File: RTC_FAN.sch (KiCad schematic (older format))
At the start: 13 parts

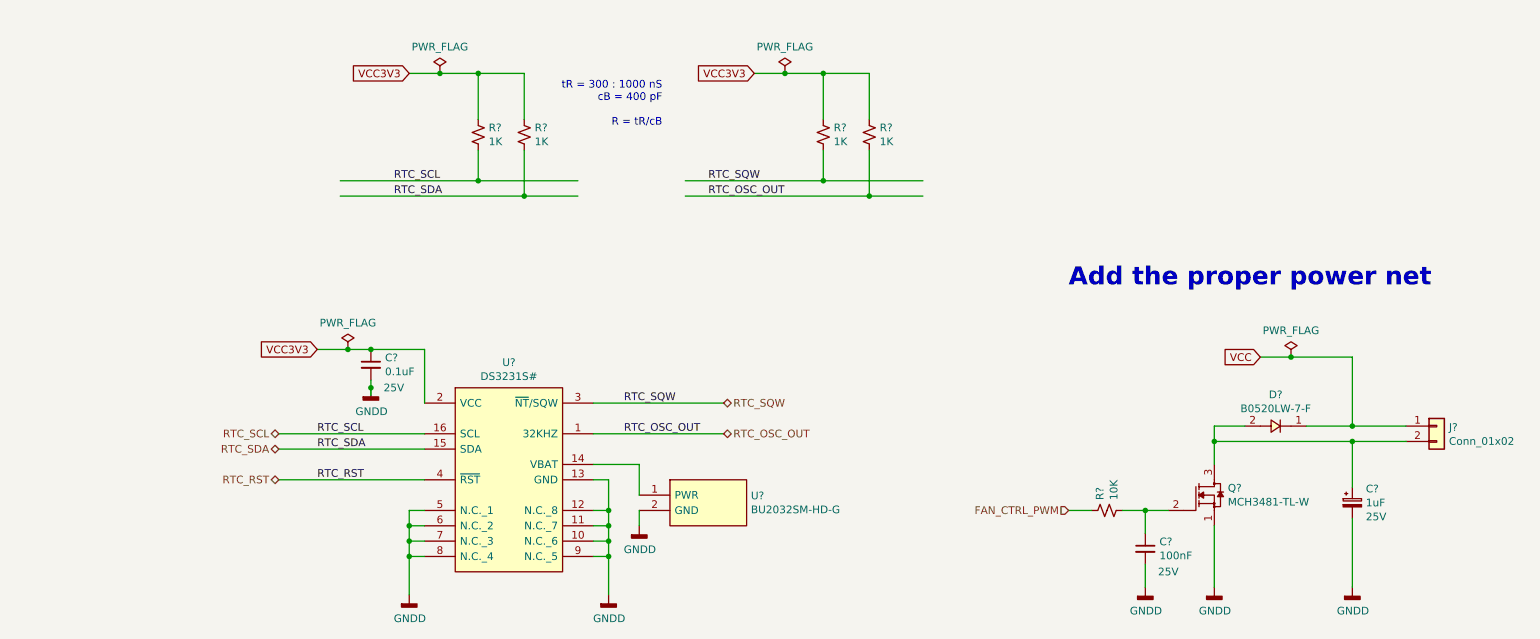
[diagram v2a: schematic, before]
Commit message: Added USB SRAM sheet,Added USB3 ethernet ic
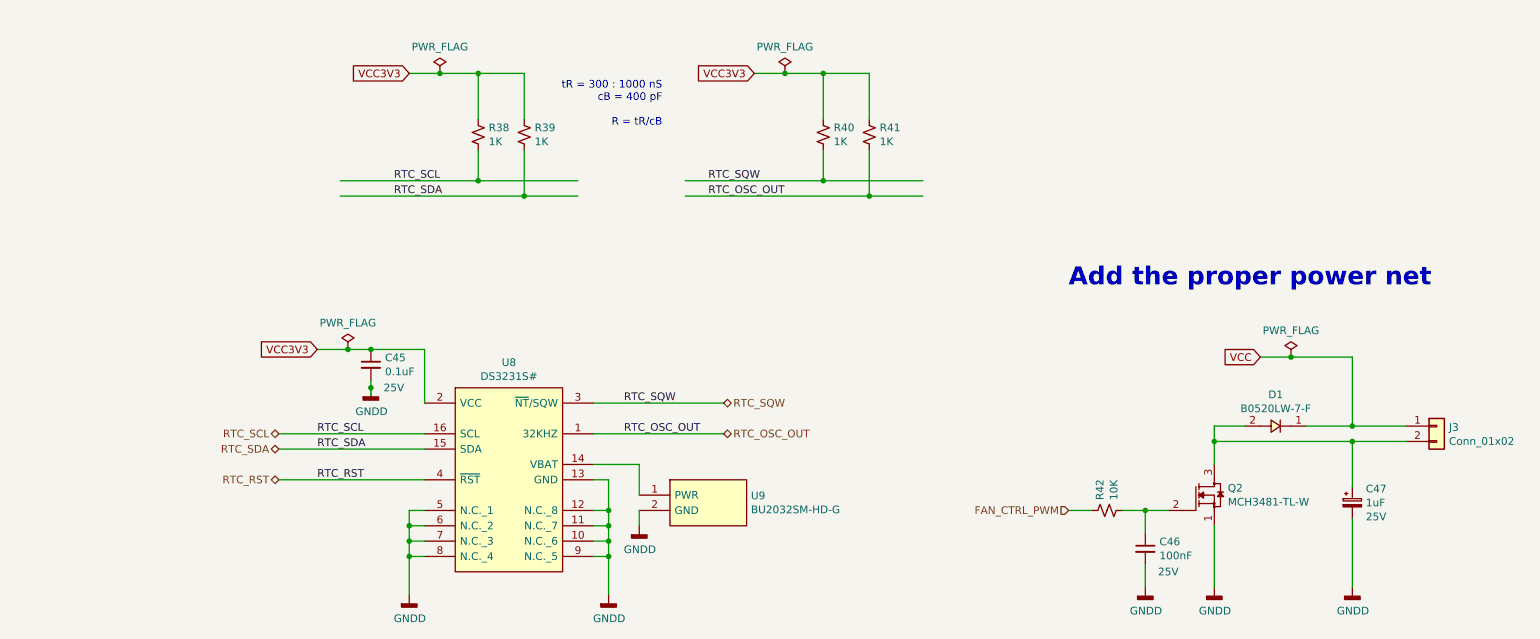
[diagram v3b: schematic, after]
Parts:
- gave numbers to parts that had none: 13
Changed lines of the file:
@@
 $Descr A4 11693 8268
 encoding utf-8
-Sheet 12 15
+Sheet 15 17
 Title "CGMPCX1006"
 Date "2021-02-03"
@@
 $EndDescr
 $Comp
-L GM_Clock_n_Timers:DS3231S# U?
+L GM_Clock_n_Timers:DS3231S# U8
 U 1 1 60229CED
 P 3400 3000
-F 0 "U?" H 3750 3165 50  0000 C CNN
+F 0 "U8" H 3750 3165 50  0000 C CNN
 F 1 "DS3231S#" H 3750 3074 50  0000 C CNN
 F 2 "SOIC127P1032X265-16N" H 4850 2700 50  0001 L CNN
@@
 AR Path="/601DF0A6/6022EFDE" Ref="#PWR?"  Part="1"
 AR Path="/601E7C5A/6022EFDE" Ref="#PWR?"  Part="1"
-AR Path="/601E7CC8/6022EFDE" Ref="#PWR?"  Part="1"
-F 0 "#PWR?" H 3100 4100 50  0001 C CNN
+AR Path="/601E7CC8/6022EFDE" Ref="#PWR029"  Part="1"
+F 0 "#PWR029" H 3100 4100 50  0001 C CNN
 F 1 "GNDD" H 3104 4195 50  0000 C CNN
 F 2 "" H 3100 4350 50  0001 C CNN
@@
 AR Path="/601DF0A6/6022F29E" Ref="#PWR?"  Part="1"
 AR Path="/601E7C5A/6022F29E" Ref="#PWR?"  Part="1"
-AR Path="/601E7CC8/6022F29E" Ref="#PWR?"  Part="1"
-F 0 "#PWR?" H 4400 4100 50  0001 C CNN
+AR Path="/601E7CC8/6022F29E" Ref="#PWR030"  Part="1"
+F 0 "#PWR030" H 4400 4100 50  0001 C CNN
 F 1 "GNDD" H 4404 4195 50  0000 C CNN
 F 2 "" H 4400 4350 50  0001 C CNN
@@
 P 2700 2750
 AR Path="/601E7C5A/6023071D" Ref="#FLG?"  Part="1"
-AR Path="/601E7CC8/6023071D" Ref="#FLG?"  Part="1"
-F 0 "#FLG?" H 2700 2825 50  0001 C CNN
+AR Path="/601E7CC8/6023071D" Ref="#FLG016"  Part="1"
+F 0 "#FLG016" H 2700 2825 50  0001 C CNN
 F 1 "PWR_FLAG" H 2700 2923 50  0000 C CNN
 F 2 "" H 2700 2750 50  0001 C CNN
@@
 P 2850 2850
 AR Path="/601E7C5A/60231765" Ref="C?"  Part="1"
-AR Path="/601E7CC8/60231765" Ref="C?"  Part="1"
-F 0 "C?" H 2942 2896 50  0000 L CNN
+AR Path="/601E7CC8/60231765" Ref="C45"  Part="1"
+F 0 "C45" H 2942 2896 50  0000 L CNN
 F 1 "0.1uF" H 2942 2805 50  0000 L CNN
 F 2 "Capacitor_SMD:C_0603_1608Metric_Pad1.08x0.95mm_HandSolder" H 2850 2850 50  0001 C CNN
@@
 AR Path="/601DF0A6/6023262F" Ref="#PWR?"  Part="1"
 AR Path="/601E7C5A/6023262F" Ref="#PWR?"  Part="1"
-AR Path="/601E7CC8/6023262F" Ref="#PWR?"  Part="1"
-F 0 "#PWR?" H 2850 2750 50  0001 C CNN
+AR Path="/601E7CC8/6023262F" Ref="#PWR028"  Part="1"
+F 0 "#PWR028" H 2850 2750 50  0001 C CNN
 F 1 "GNDD" H 2854 2845 50  0000 C CNN
 F 2 "" H 2850 3000 50  0001 C CNN
@@
 P 3300 950
 AR Path="/601E7C5A/602351EC" Ref="#FLG?"  Part="1"
-AR Path="/601E7CC8/602351EC" Ref="#FLG?"  Part="1"
-F 0 "#FLG?" H 3300 1025 50  0001 C CNN
+AR Path="/601E7CC8/602351EC" Ref="#FLG017"  Part="1"
+F 0 "#FLG017" H 3300 1025 50  0001 C CNN
 F 1 "PWR_FLAG" H 3300 1123 50  0000 C CNN
 F 2 "" H 3300 950 50  0001 C CNN
@@
 P 3550 1350
 AR Path="/601E7C5A/60235A7C" Ref="R?"  Part="1"
-AR Path="/601E7CC8/60235A7C" Ref="R?"  Part="1"
-F 0 "R?" H 3618 1396 50  0000 L CNN
+AR Path="/601E7CC8/60235A7C" Ref="R38"  Part="1"
+F 0 "R38" H 3618 1396 50  0000 L CNN
 F 1 "1K" H 3618 1305 50  0000 L CNN
 F 2 "Resistor_SMD:R_0603_1608Metric_Pad0.98x0.95mm_HandSolder" H 3550 1350 50  0001 C CNN
@@
 P 3850 1350
 AR Path="/601E7C5A/60236293" Ref="R?"  Part="1"
-AR Path="/601E7CC8/60236293" Ref="R?"  Part="1"
-F 0 "R?" H 3918 1396 50  0000 L CNN
+AR Path="/601E7CC8/60236293" Ref="R39"  Part="1"
+F 0 "R39" H 3918 1396 50  0000 L CNN
 F 1 "1K" H 3918 1305 50  0000 L CNN
 F 2 "Resistor_SMD:R_0603_1608Metric_Pad0.98x0.95mm_HandSolder" H 3850 1350 50  0001 C CNN
@@
 P 5550 950
 AR Path="/601E7C5A/6024882C" Ref="#FLG?"  Part="1"
-AR Path="/601E7CC8/6024882C" Ref="#FLG?"  Part="1"
-F 0 "#FLG?" H 5550 1025 50  0001 C CNN
+AR Path="/601E7CC8/6024882C" Ref="#FLG018"  Part="1"
+F 0 "#FLG018" H 5550 1025 50  0001 C CNN
 F 1 "PWR_FLAG" H 5550 1123 50  0000 C CNN
 F 2 "" H 5550 950 50  0001 C CNN
@@
 P 5800 1350
 AR Path="/601E7C5A/60248834" Ref="R?"  Part="1"
-AR Path="/601E7CC8/60248834" Ref="R?"  Part="1"
-F 0 "R?" H 5868 1396 50  0000 L CNN
+AR Path="/601E7CC8/60248834" Ref="R40"  Part="1"
+F 0 "R40" H 5868 1396 50  0000 L CNN
 F 1 "1K" H 5868 1305 50  0000 L CNN
 F 2 "Resistor_SMD:R_0603_1608Metric_Pad0.98x0.95mm_HandSolder" H 5800 1350 50  0001 C CNN
@@
 P 6100 1350
 AR Path="/601E7C5A/6024883A" Ref="R?"  Part="1"
-AR Path="/601E7CC8/6024883A" Ref="R?"  Part="1"
-F 0 "R?" H 6168 1396 50  0000 L CNN
+AR Path="/601E7CC8/6024883A" Ref="R41"  Part="1"
+F 0 "R41" H 6168 1396 50  0000 L CNN
 F 1 "1K" H 6168 1305 50  0000 L CNN
 F 2 "Resistor_SMD:R_0603_1608Metric_Pad0.98x0.95mm_HandSolder" H 6100 1350 50  0001 C CNN
@@
 AR Path="/601DF0A6/6025F3F3" Ref="#PWR?"  Part="1"
 AR Path="/601E7C5A/6025F3F3" Ref="#PWR?"  Part="1"
-AR Path="/601E7CC8/6025F3F3" Ref="#PWR?"  Part="1"
-F 0 "#PWR?" H 4600 3650 50  0001 C CNN
+AR Path="/601E7CC8/6025F3F3" Ref="#PWR031"  Part="1"
+F 0 "#PWR031" H 4600 3650 50  0001 C CNN
 F 1 "GNDD" H 4604 3745 50  0000 C CNN
 F 2 "" H 4600 3900 50  0001 C CNN
@@
 $EndComp
 $Comp
-L GM_Battery_Holders_n_Contacts:BU2032SM-HD-G U?
+L GM_Battery_Holders_n_Contacts:BU2032SM-HD-G U9
 U 1 1 6022F346
 P 4800 3600
-F 0 "U?" H 5328 3496 50  0000 L CNN
+F 0 "U9" H 5328 3496 50  0000 L CNN
 F 1 "BU2032SM-HD-G" H 5328 3405 50  0000 L CNN
 F 2 "BU2032SM-HD-G" H 5450 3700 50  0001 L CNN
@@
 	4600 3500 4300 3500
 $Comp
-L GM_MOSFET:MCH3481-TL-W Q?
+L GM_MOSFET:MCH3481-TL-W Q2
 U 1 1 602539F0
 P 8250 3700
-F 0 "Q?" H 8438 3746 50  0000 L CNN
+F 0 "Q2" H 8438 3746 50  0000 L CNN
 F 1 "MCH3481-TL-W" H 8438 3655 50  0000 L CNN
 F 2 "GM_SOT:SOT65P270X085-3N" H 9250 3900 50  0001 C CNN
@@
 P 7650 3800
 AR Path="/601E7C5A/60254F0F" Ref="R?"  Part="1"
-AR Path="/601E7CC8/60254F0F" Ref="R?"  Part="1"
-F 0 "R?" H 7718 3846 50  0000 L CNN
+AR Path="/601E7CC8/60254F0F" Ref="R42"  Part="1"
+F 0 "R42" H 7718 3846 50  0000 L CNN
 F 1 "10K" H 7718 3755 50  0000 L CNN
 F 2 "Resistor_SMD:R_0603_1608Metric_Pad0.98x0.95mm_HandSolder" H 7650 3800 50  0001 C CNN
@@
 P 7900 4050
 AR Path="/601E7C5A/60254F16" Ref="C?"  Part="1"
-AR Path="/601E7CC8/60254F16" Ref="C?"  Part="1"
-F 0 "C?" H 7992 4096 50  0000 L CNN
+AR Path="/601E7CC8/60254F16" Ref="C46"  Part="1"
+F 0 "C46" H 7992 4096 50  0000 L CNN
 F 1 "100nF" H 7992 4005 50  0000 L CNN
 F 2 "Capacitor_SMD:C_0603_1608Metric_Pad1.08x0.95mm_HandSolder" H 7900 4050 50  0001 C CNN
@@
 AR Path="/601DF0A6/6025D5E9" Ref="#PWR?"  Part="1"
 AR Path="/601E7C5A/6025D5E9" Ref="#PWR?"  Part="1"
-AR Path="/601E7CC8/6025D5E9" Ref="#PWR?"  Part="1"
-F 0 "#PWR?" H 7900 4050 50  0001 C CNN
+AR Path="/601E7CC8/6025D5E9" Ref="#PWR032"  Part="1"
+F 0 "#PWR032" H 7900 4050 50  0001 C CNN
 F 1 "GNDD" H 7904 4145 50  0000 C CNN
 F 2 "" H 7900 4300 50  0001 C CNN
@@
 AR Path="/601DF0A6/60263673" Ref="#PWR?"  Part="1"
 AR Path="/601E7C5A/60263673" Ref="#PWR?"  Part="1"
-AR Path="/601E7CC8/60263673" Ref="#PWR?"  Part="1"
-F 0 "#PWR?" H 8350 4050 50  0001 C CNN
+AR Path="/601E7CC8/60263673" Ref="#PWR033"  Part="1"
+F 0 "#PWR033" H 8350 4050 50  0001 C CNN
 F 1 "GNDD" H 8354 4145 50  0000 C CNN
 F 2 "" H 8350 4300 50  0001 C CNN
@@
 $EndComp
 $Comp
-L Device:C_Polarized_Small C?
+L Device:C_Polarized_Small C47
 U 1 1 60269FC6
 P 9250 3750
-F 0 "C?" H 9338 3841 50  0000 L CNN
+F 0 "C47" H 9338 3841 50  0000 L CNN
 F 1 "1uF" H 9338 3750 50  0000 L CNN
 F 2 "Capacitor_Tantalum_SMD:CP_EIA-1608-10_AVX-L_Pad1.25x1.05mm_HandSolder" H 9250 3750 50  0001 C CNN
@@
 $EndComp
 $Comp
-L Connector_Generic:Conn_01x02 J?
+L Connector_Generic:Conn_01x02 J3
 U 1 1 60278B21
 P 9800 3250
-F 0 "J?" H 9880 3242 50  0000 L CNN
+F 0 "J3" H 9880 3242 50  0000 L CNN
 F 1 "Conn_01x02" H 9880 3151 50  0000 L CNN
 F 2 "Connector_PinHeader_1.27mm:PinHeader_1x02_P1.27mm_Vertical" H 9800 3250 50  0001 C CNN
@@
 AR Path="/601DF0A6/6028129F" Ref="#PWR?"  Part="1"
 AR Path="/601E7C5A/6028129F" Ref="#PWR?"  Part="1"
-AR Path="/601E7CC8/6028129F" Ref="#PWR?"  Part="1"
-F 0 "#PWR?" H 9250 4050 50  0001 C CNN
+AR Path="/601E7CC8/6028129F" Ref="#PWR034"  Part="1"
+F 0 "#PWR034" H 9250 4050 50  0001 C CNN
 F 1 "GNDD" H 9254 4145 50  0000 C CNN
 F 2 "" H 9250 4300 50  0001 C CNN
@@
 	7550 3800 7400 3800
 $Comp
-L GM_Diodes:B0520LW-7-F D?
+L GM_Diodes:B0520LW-7-F D1
 U 1 1 6029EC80
 P 8750 3250
-F 0 "D?" H 8750 3045 50  0000 C CNN
+F 0 "D1" H 8750 3045 50  0000 C CNN
 F 1 "B0520LW-7-F" H 8750 3136 50  0000 C CNN
 F 2 "SOD3716X145N" H 9250 3250 50  0001 L CNN
@@
 P 8850 2800
 AR Path="/601E7C5A/602A4D12" Ref="#FLG?"  Part="1"
-AR Path="/601E7CC8/602A4D12" Ref="#FLG?"  Part="1"
-F 0 "#FLG?" H 8850 2875 50  0001 C CNN
+AR Path="/601E7CC8/602A4D12" Ref="#FLG019"  Part="1"
+F 0 "#FLG019" H 8850 2875 50  0001 C CNN
 F 1 "PWR_FLAG" H 8850 2973 50  0000 C CNN
 F 2 "" H 8850 2800 50  0001 C CNN

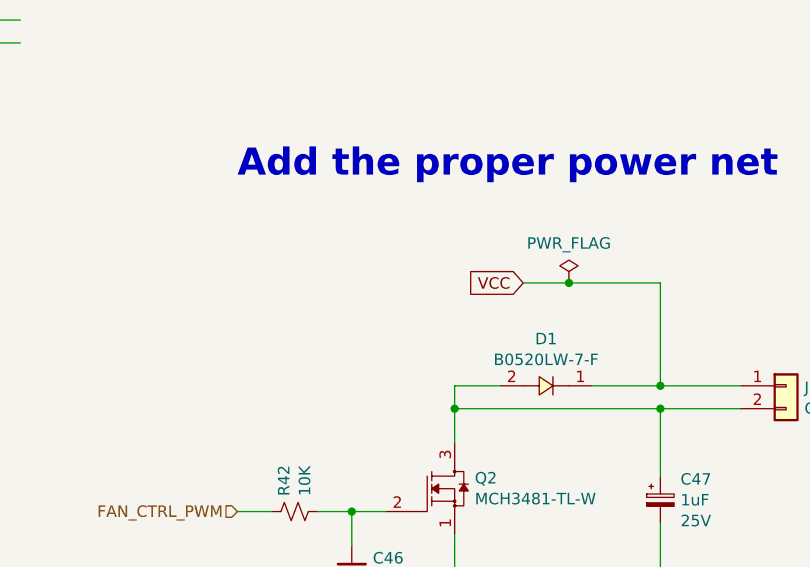
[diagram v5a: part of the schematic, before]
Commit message: Added bus lines -ETH_PHY_CONN -RAM -USB2 Made Output the port direction of clkout of Clock_Gen Placed sheet entris of sheet symbols on top sheet
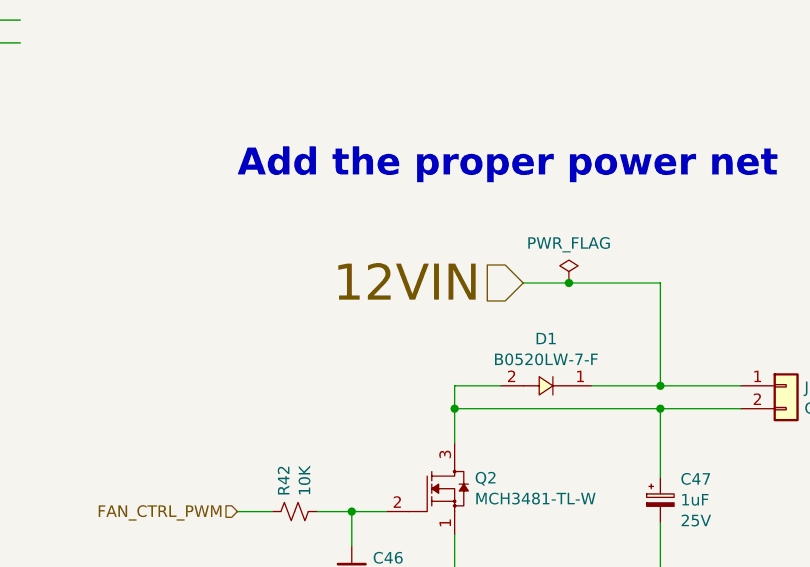
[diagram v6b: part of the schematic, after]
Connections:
- net labels added: 12VIN
- net labels removed: VCC
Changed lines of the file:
@@
 $Descr A4 11693 8268
 encoding utf-8
-Sheet 12 19
+Sheet 11 20
 Title "CGMPCX1006"
 Date "2021-02-03"
@@
 	8350 3250 8350 3350
 Connection ~ 8350 3350
-Text GLabel 8650 2800 0    50   Input ~ 0
-VCC
 $Comp
 L power:PWR_FLAG #FLG?
@@
 Text Notes 7400 2350 0    118  ~ 24
 Add the proper power net
+Text HLabel 8650 2800 0    157  Input ~ 0
+12VIN
 $EndSCHEMATC
